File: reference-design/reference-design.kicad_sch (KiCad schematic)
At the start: 21 parts

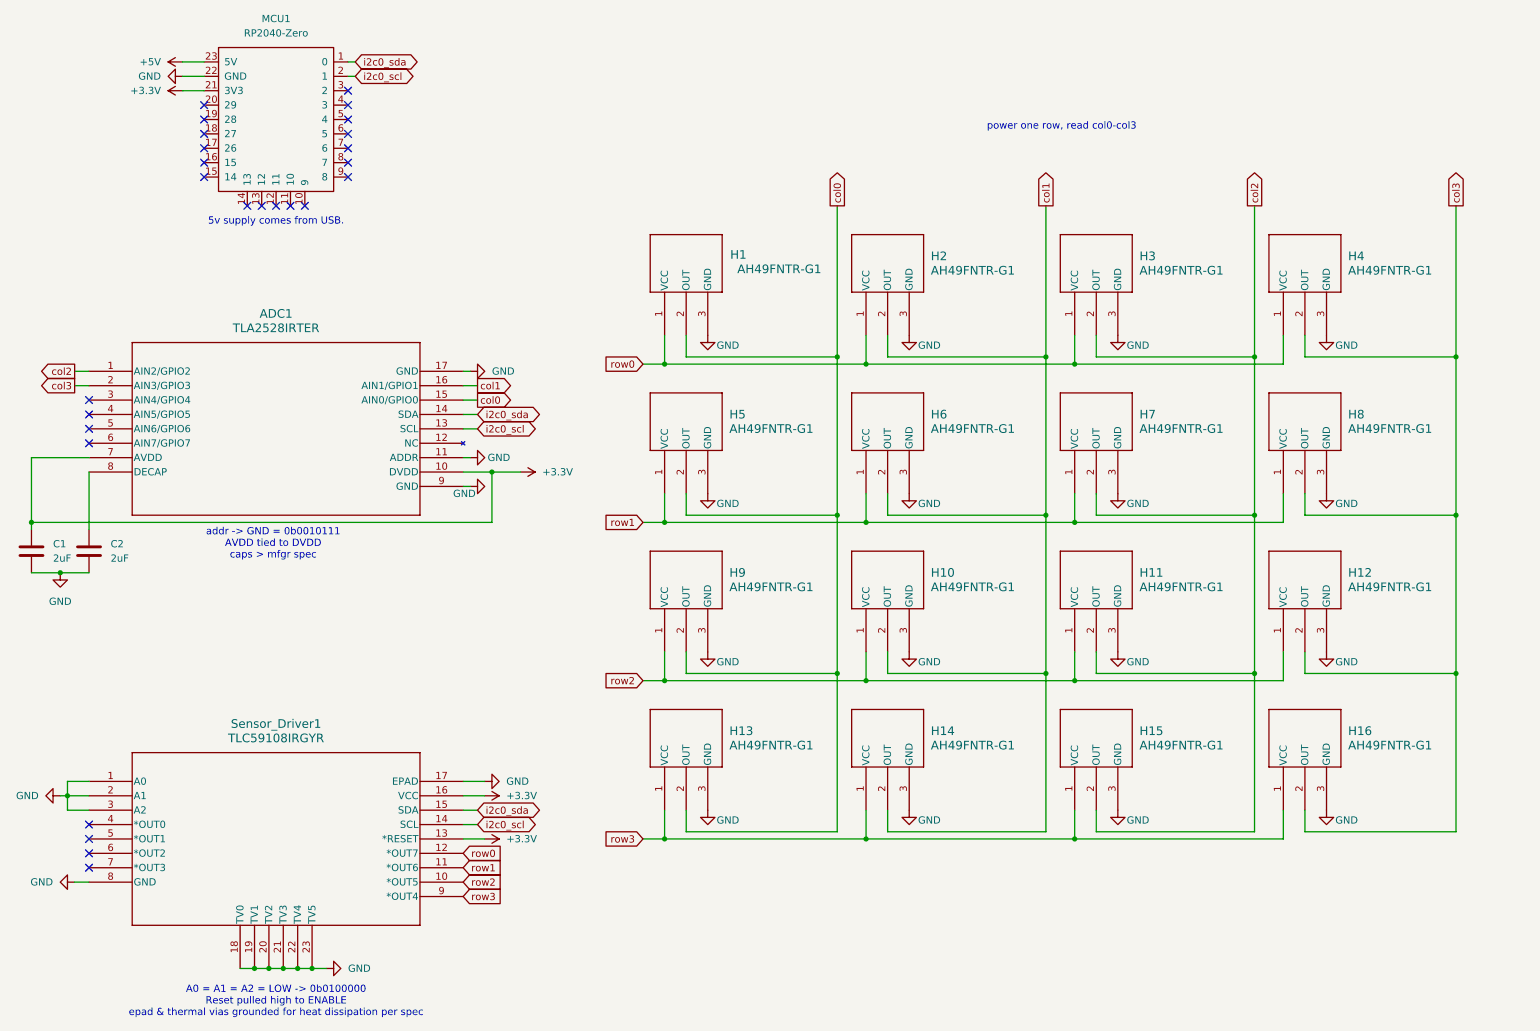
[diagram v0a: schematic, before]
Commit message: add testpoints
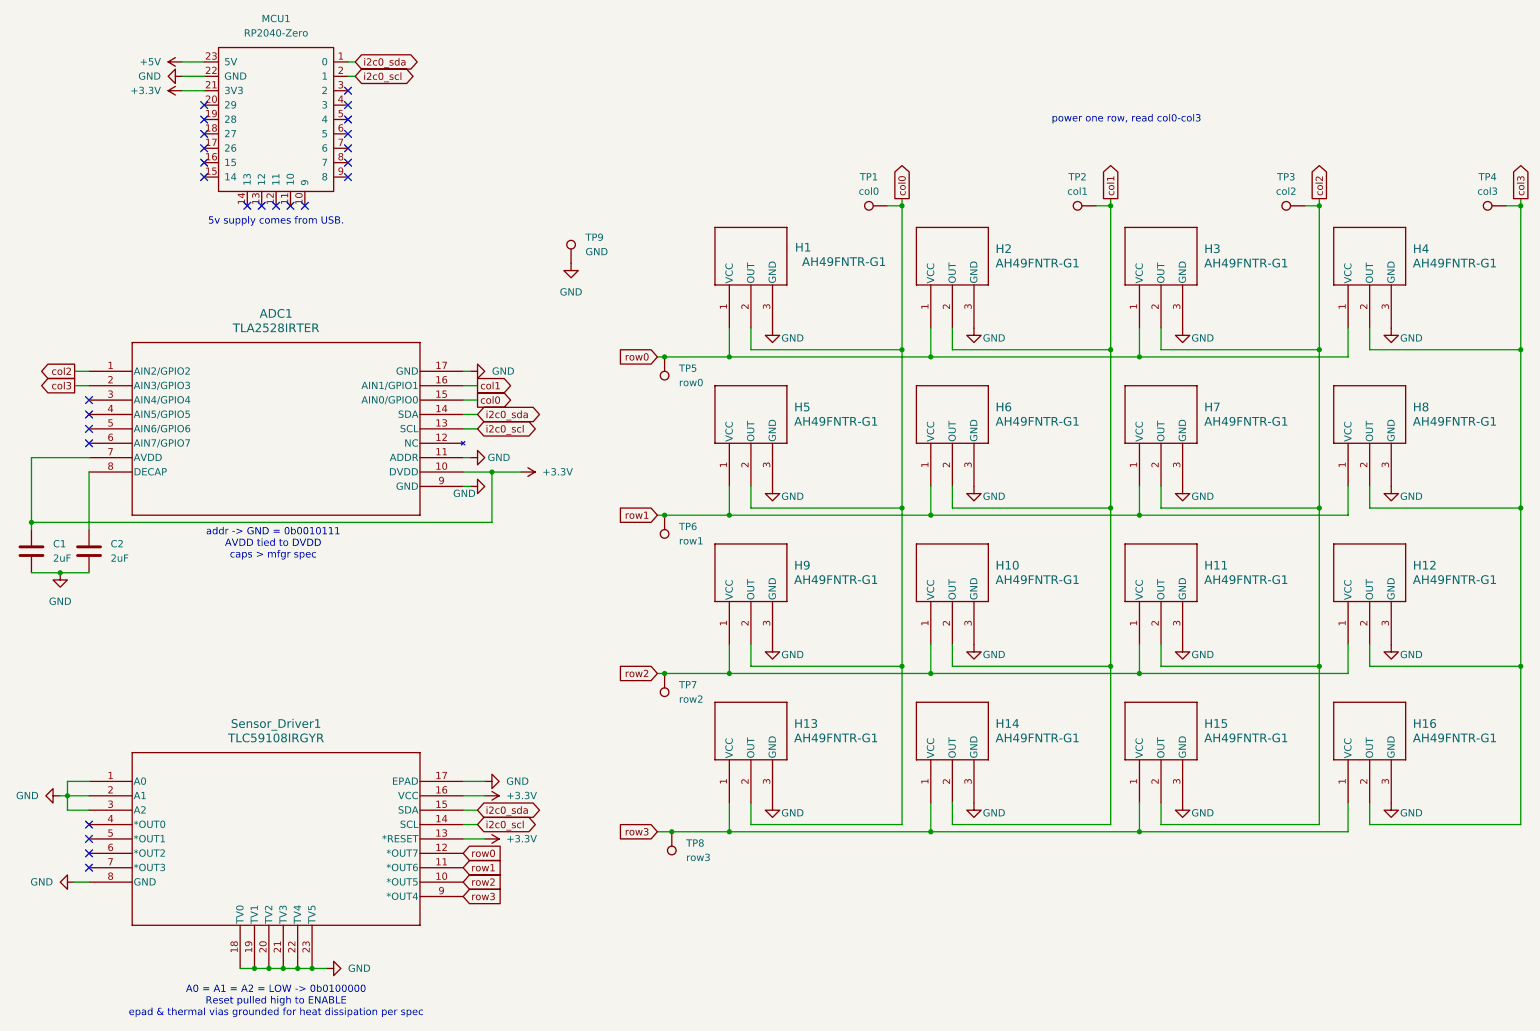
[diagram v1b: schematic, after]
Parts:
- added TP1: col0, TestPoint:TestPoint_Pad_2.0x2.0mm, symbol Connector:TestPoint
- added TP2: col1, TestPoint:TestPoint_Pad_2.0x2.0mm, symbol Connector:TestPoint
- added TP3: col2, TestPoint:TestPoint_Pad_2.0x2.0mm, symbol Connector:TestPoint
- added TP4: col3, TestPoint:TestPoint_Pad_2.0x2.0mm, symbol Connector:TestPoint
- added TP5: row0, TestPoint:TestPoint_Pad_2.0x2.0mm, symbol Connector:TestPoint
- added TP6: row1, TestPoint:TestPoint_Pad_2.0x2.0mm, symbol Connector:TestPoint
- added TP7: row2, TestPoint:TestPoint_Pad_2.0x2.0mm, symbol Connector:TestPoint
- added TP8: row3, TestPoint:TestPoint_Pad_2.0x2.0mm, symbol Connector:TestPoint
- added TP9: GND, TestPoint:TestPoint_Pad_2.0x2.0mm, symbol Connector:TestPoint
- Sensor_Driver1: footprint RGY16_2P55X2P05 -> TLC59208FIRGYR:RGY16_2P55X2P05
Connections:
- net GND: now also TP9.1
- net col0: now also TP1.1
- net col1: now also TP2.1
- net col2: now also TP3.1
- net col3: now also TP4.1
- net row0: now also TP5.1
- net row1: now also TP6.1
- net row2: now also TP7.1
- net row3: now also TP8.1
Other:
- moved on the sheet: H1, H10, H11, H12, H13, H14, H15, H16, H2, H3, H4, H5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
